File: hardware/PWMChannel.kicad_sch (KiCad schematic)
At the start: 4 parts, among them Q201 IQE006NE2LM5CGSC

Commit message: Refresh
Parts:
- C201: footprint Capacitor_SMD:C_0603_1608Metric -> V2_Capacitor_SMD:C_0603; symbol Device:C_Small -> V2_Device:C_0603_0u1; Manufacturer (none) -> TDK; Mouser (none) -> 810-CGA3E2X7R1H104MA; Product (none) -> CGA3E2X7R1H104M080AA
- D201: footprint Diode_SMD:D_SOD-123F -> V2_Diode_SMD:D_SOD-123F; Manufacturer (none) -> onsemi; Mouser (none) -> 512-S310FA; Product (none) -> S310FA
- D202: LCSC (none) -> C965555; Manufacturer (none) -> Worldsemi; Product (none) -> WS2812B-2020
- Q201: value IQE006NE2LM5CGSC -> IQE022N06LM5CGSCATMA1; symbol V2_Transistor_FET:IQE006NE2LM5CGSC -> V2_Transistor_FET:IQE022N06LM5CGSCATMA1; Manufacturer (none) -> Infineon Technologies; Mouser (none) -> 726-IQE006NE2LM5CGSC; Product (none) -> IQE006NE2LM5CGSCATMA1
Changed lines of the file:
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@@
 			)
 		)
-		(property "Footprint" "Diode_SMD:D_SOD-123F"
+		(property "Footprint" "V2_Diode_SMD:D_SOD-123F"
 			(at 139.065 88.9 0)
 			(effects
@@
 		(property "Description" ""
 			(at 146.05 88.9 0)
+			(effects
+				(font
+					(size 1.27 1.27)
+				)
+				(hide yes)
+			)
+		)
+		(property "Mouser" "512-S310FA"
+			(at 130.81 88.9 0)
+			(effects
+				(font
+					(size 1.27 1.27)
+				)
+				(hide yes)
+			)
+		)
+		(property "Manufacturer" "onsemi"
+			(at 135.89 88.9 0)
+			(effects
+				(font
+					(size 1.27 1.27)
+				)
+				(hide yes)
+			)
+		)
+		(property "Product" "S310FA"
+			(at 133.35 88.9 0)
+			(effects
+				(font
+					(size 1.27 1.27)
+				)
+				(hide yes)
+			)
+		)
+		(property "Sim.Pin" ""
+			(at 146.05 88.9 90)
 			(effects
 				(font
@@
 	)
 	(symbol
-		(lib_id "Device:C_Small")
+		(lib_id "V2_Device:C_0603_0u1")
 		(at 133.35 88.9 0)
 		(unit 1)
@@
 			)
 		)
-		(property "Footprint" "Capacitor_SMD:C_0603_1608Metric"
+		(property "Footprint" "V2_Capacitor_SMD:C_0603"
+			(at 133.35 105.918 0)
+			(effects
+				(font
+					(size 1.27 1.27)
+				)
+				(hide yes)
+			)
+		)
+		(property "Datasheet" ""
 			(at 133.35 88.9 0)
 			(effects
@@
 			)
 		)
-		(property "Datasheet" "~"
-			(at 133.35 88.9 0)
-			(effects
-				(font
-					(size 1.27 1.27)
-				)
-				(hide yes)
-			)
-		)
 		(property "Description" "Unpolarized capacitor, small symbol"
+			(at 133.35 101.6 0)
+			(effects
+				(font
+					(size 1.27 1.27)
+				)
+				(hide yes)
+			)
+		)
+		(property "Mouser" "810-CGA3E2X7R1H104MA"
+			(at 133.35 109.22 0)
+			(show_name yes)
+			(effects
+				(font
+					(size 1.27 1.27)
+				)
+				(hide yes)
+			)
+		)
+		(property "Manufacturer" "TDK"
+			(at 133.35 104.14 0)
+			(show_name yes)
+			(effects
+				(font
+					(size 1.27 1.27)
+				)
+				(hide yes)
+			)
+		)
+		(property "Product" "CGA3E2X7R1H104M080AA"
+			(at 133.35 106.68 0)
+			(show_name yes)
+			(effects
+				(font
+					(size 1.27 1.27)
+				)
+				(hide yes)
+			)
+		)
+		(property "Sim.Pin" ""
 			(at 133.35 88.9 0)
 			(effects
@@
 	)
 	(symbol
-		(lib_id "V2_Transistor_FET:IQE006NE2LM5CGSC")
+		(lib_id "V2_Transistor_FET:IQE022N06LM5CGSCATMA1")
 		(at 130.81 96.52 0)
 		(unit 1)
@@
 			)
 		)
-		(property "Value" "IQE006NE2LM5CGSC"
-			(at 137.16 98.425 0)
+		(property "Value" "IQE022N06LM5CGSCATMA1"
+			(at 137.16 98.044 0)
 			(effects
 				(font
@@
 		)
 		(property "Description" ""
+			(at 130.81 96.52 0)
+			(effects
+				(font
+					(size 1.27 1.27)
+				)
+				(hide yes)
+			)
+		)
+		(property "Mouser" "726-IQE006NE2LM5CGSC"
+			(at 130.81 119.38 0)
+			(effects
+				(font
+					(size 1.27 1.27)
+				)
+				(hide yes)
+			)
+		)
+		(property "Product" "IQE006NE2LM5CGSCATMA1"
+			(at 130.81 116.84 0)
+			(effects
+				(font
+					(size 1.27 1.27)
+				)
+				(hide yes)
+			)
+		)
+		(property "Manufacturer" "Infineon Technologies"
+			(at 130.81 114.3 0)
+			(effects
+				(font
+					(size 1.27 1.27)
+				)
+				(hide yes)
+			)
+		)
+		(property "Sim.Pin" ""
 			(at 130.81 96.52 0)
 			(effects
@@
 	)
 	(symbol
-		(lib_id "power:GND")
+		(lib_id "V2_power:GND")
 		(at 160.02 127 90)
 		(unit 1)
@@
 			)
 		)
+		(property "Manufacturer" "Worldsemi"
+			(at 152.4 141.224 0)
+			(effects
+				(font
+					(size 1.27 1.27)
+				)
+				(hide yes)
+			)
+		)
+		(property "Product" "WS2812B-2020"
+			(at 152.4 138.684 0)
+			(effects
+				(font
+					(size 1.27 1.27)
+				)
+				(hide yes)
+			)
+		)
+		(property "LCSC" "C965555"
+			(at 152.4 144.018 0)
+			(effects
+				(font
+					(size 1.27 1.27)
+				)
+				(hide yes)
+			)
+		)
+		(property "Sim.Pin" ""
+			(at 152.4 125.73 0)
+			(effects
+				(font
+					(size 1.27 1.27)
+				)
+				(hide yes)
+			)
+		)
 		(pin "1"
 		)
@@
 	)
 	(symbol
-		(lib_id "power:GND")
+		(lib_id "V2_power:GND")
 		(at 133.35 101.6 0)
 		(unit 1)
@@
 	)
 	(symbol
-		(lib_id "power:+5V")
+		(lib_id "V2_power:+5V")
 		(at 160.02 121.92 270)
 		(unit 1)

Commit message: Refresh
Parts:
- Q201: value IQE022N06LM5CGSCATMA1 -> IQE006NE2LM5CGSC; symbol V2_Transistor_FET:IQE022N06LM5CGSCATMA1 -> V2_Transistor_FET:IQE006NE2LM5CGSC; Polarity (none) -> N; Product IQE006NE2LM5CGSCATMA1 -> IQE006NE2LM5CGSC; Rating (none) -> 25V
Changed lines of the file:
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@@
-			)
-		)
-		(property "Sim.Pin" ""
-			(at 146.05 88.9 90)
-			(effects
-				(font
-					(size 1.27 1.27)
-				)
-				(hide yes)
 			)
 		)
@@
 			)
 		)
-		(property "Sim.Pin" ""
-			(at 133.35 88.9 0)
-			(effects
-				(font
-					(size 1.27 1.27)
-				)
-				(hide yes)
-			)
-		)
 		(pin "1"
 		)
@@
 	)
 	(symbol
-		(lib_id "V2_Transistor_FET:IQE022N06LM5CGSCATMA1")
+		(lib_id "V2_Transistor_FET:IQE006NE2LM5CGSC")
 		(at 130.81 96.52 0)
 		(unit 1)
@@
 			)
 		)
-		(property "Value" "IQE022N06LM5CGSCATMA1"
-			(at 137.16 98.044 0)
+		(property "Value" "IQE006NE2LM5CGSC"
+			(at 135.89 96.52 0)
 			(effects
 				(font
@@
 		)
 		(property "Footprint" "V2_Package_TFN:WHTFN-9"
-			(at 135.89 98.425 0)
-			(effects
-				(font
-					(size 1.27 1.27)
-				)
-				(justify left)
+			(at 130.81 113.03 0)
+			(show_name yes)
+			(effects
+				(font
+					(size 1.27 1.27)
+				)
 				(hide yes)
 			)
@@
 		)
 		(property "Mouser" "726-IQE006NE2LM5CGSC"
+			(at 130.81 124.46 0)
+			(show_name yes)
+			(effects
+				(font
+					(size 1.27 1.27)
+				)
+				(hide yes)
+			)
+		)
+		(property "Product" "IQE006NE2LM5CGSC"
+			(at 130.81 121.92 0)
+			(show_name yes)
+			(effects
+				(font
+					(size 1.27 1.27)
+				)
+				(hide yes)
+			)
+		)
+		(property "Manufacturer" "Infineon Technologies"
 			(at 130.81 119.38 0)
-			(effects
-				(font
-					(size 1.27 1.27)
-				)
-				(hide yes)
-			)
-		)
-		(property "Product" "IQE006NE2LM5CGSCATMA1"
-			(at 130.81 116.84 0)
-			(effects
-				(font
-					(size 1.27 1.27)
-				)
-				(hide yes)
-			)
-		)
-		(property "Manufacturer" "Infineon Technologies"
-			(at 130.81 114.3 0)
+			(show_name yes)
 			(effects
 				(font
@@
 		(property "Sim.Pin" ""
 			(at 130.81 96.52 0)
+			(effects
+				(font
+					(size 1.27 1.27)
+				)
+				(hide yes)
+			)
+		)
+		(property "Rating" "25V"
+			(at 130.81 116.84 0)
+			(effects
+				(font
+					(size 1.27 1.27)
+				)
+				(hide yes)
+			)
+		)
+		(property "Polarity" "N"
+			(at 130.81 114.3 0)
 			(effects
 				(font
@@
 			(effects
 				(font
-					(size 1.27 1.27)
-				)
-				(hide yes)
-			)
-		)
-		(property "Sim.Pin" ""
-			(at 152.4 125.73 0)
-			(effects
-				(font

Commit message: Update library
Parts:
- C201: Rating (none) -> 50V
- Q201: value IQE006NE2LM5CGSC -> IQE006NE2LM5CG; symbol V2_Transistor_FET:IQE006NE2LM5CGSC -> V2_Transistor_FET:IQE006NE2LM5CG; Mouser 726-IQE006NE2LM5CGSC -> 726-IQE006NE2LM5CGAT; Product IQE006NE2LM5CGSC -> IQE006NE2LM5CG
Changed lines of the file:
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@@
+			)
+		)
+		(property "Sim.Pin" ""
+			(at 146.05 88.9 90)
+			(effects
+				(font
+					(size 1.27 1.27)
+				)
+				(hide yes)
+			)
+		)
+		(property "Voltage" ""
+			(at 146.05 88.9 90)
+			(effects
+				(font
+					(size 1.27 1.27)
+				)
+				(hide yes)
 			)
 		)
@@
 			)
 		)
+		(property "Rating" "50V"
+			(at 133.35 111.76 0)
+			(effects
+				(font
+					(size 1.27 1.27)
+				)
+				(hide yes)
+			)
+		)
+		(property "Sim.Pin" ""
+			(at 133.35 88.9 0)
+			(effects
+				(font
+					(size 1.27 1.27)
+				)
+				(hide yes)
+			)
+		)
+		(property "Voltage" ""
+			(at 133.35 88.9 0)
+			(effects
+				(font
+					(size 1.27 1.27)
+				)
+				(hide yes)
+			)
+		)
 		(pin "1"
 		)
@@
 	)
 	(symbol
-		(lib_id "V2_Transistor_FET:IQE006NE2LM5CGSC")
+		(lib_id "V2_Transistor_FET:IQE006NE2LM5CG")
 		(at 130.81 96.52 0)
 		(unit 1)
@@
 			)
 		)
-		(property "Value" "IQE006NE2LM5CGSC"
-			(at 135.89 96.52 0)
+		(property "Value" "IQE006NE2LM5CG"
+			(at 137.16 98.044 0)
 			(effects
 				(font
@@
 			)
 		)
-		(property "Mouser" "726-IQE006NE2LM5CGSC"
+		(property "Mouser" "726-IQE006NE2LM5CGAT"
 			(at 130.81 124.46 0)
 			(show_name yes)
@@
 			)
 		)
-		(property "Product" "IQE006NE2LM5CGSC"
+		(property "Product" "IQE006NE2LM5CG"
 			(at 130.81 121.92 0)
 			(show_name yes)
@@
 			)
 		)
+		(property "Rating" "25V"
+			(at 130.81 116.84 0)
+			(show_name yes)
+			(effects
+				(font
+					(size 1.27 1.27)
+				)
+				(hide yes)
+			)
+		)
+		(property "Polarity" "N"
+			(at 130.81 114.3 0)
+			(show_name yes)
+			(effects
+				(font
+					(size 1.27 1.27)
+				)
+				(hide yes)
+			)
+		)
 		(property "Sim.Pin" ""
 			(at 130.81 96.52 0)
@@
 			)
 		)
-		(property "Rating" "25V"
-			(at 130.81 116.84 0)
-			(effects
-				(font
-					(size 1.27 1.27)
-				)
-				(hide yes)
-			)
-		)
-		(property "Polarity" "N"
-			(at 130.81 114.3 0)
+		(property "Voltage" ""
+			(at 130.81 96.52 0)
 			(effects
 				(font
@@
 			)
 		)
-		(property "Description" "Power symbol creates a global label with name \"GND\" , ground"
+		(property "Description" ""
 			(at 160.02 127 0)
 			(effects
@@
 			)
 		)
+		(property "Sim.Pin" ""
+			(at 152.4 125.73 0)
+			(effects
+				(font
+					(size 1.27 1.27)
+				)
+				(hide yes)
+			)
+		)
+		(property "Voltage" ""
+			(at 152.4 125.73 0)
+			(effects
+				(font
+					(size 1.27 1.27)
+				)
+				(hide yes)
+			)
+		)
 		(pin "1"
 		)
@@
 			)
 		)
-		(property "Description" "Power symbol creates a global label with name \"GND\" , ground"
+		(property "Description" ""
 			(at 133.35 101.6 0)
 			(effects
@@
 			)
 		)
-		(property "Description" "Power symbol creates a global label with name \"+5V\""
+		(property "Description" ""
 			(at 160.02 121.92 0)
 			(effects

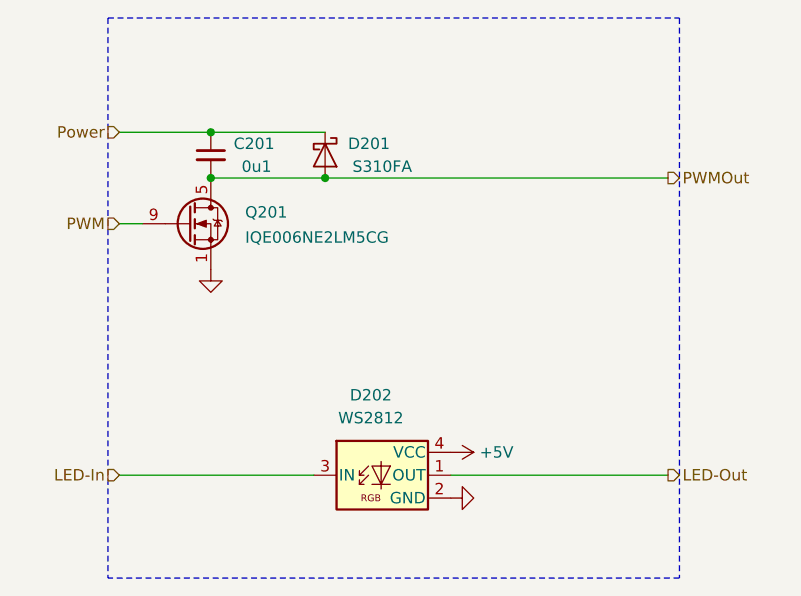
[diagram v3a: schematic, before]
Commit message: Replace Order_Number
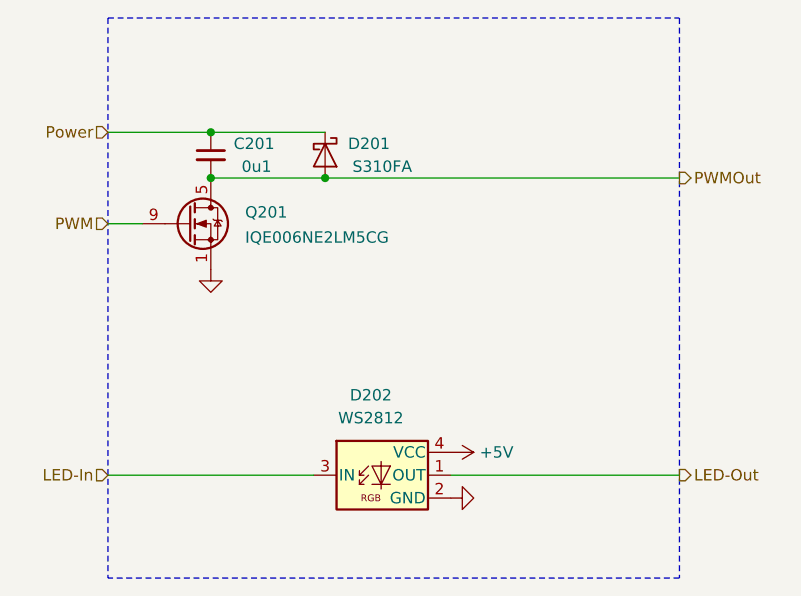
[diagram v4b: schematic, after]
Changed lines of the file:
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@@
 	(title_block
 		(title "Solenoid Channel")
-		(date "2023-01-16")
-		(rev "1")
+		(date "2026-02-10")
+		(rev "2026-02-10")
 		(company "Power MOSFET + RGB LED")
 	)
@@
 	(wire
 		(pts
-			(xy 123.19 96.52) (xy 125.73 96.52)
+			(xy 121.92 96.52) (xy 125.73 96.52)
 		)
 		(stroke
@@
 	(wire
 		(pts
-			(xy 184.15 124.46) (xy 160.02 124.46)
+			(xy 185.42 124.46) (xy 160.02 124.46)
 		)
 		(stroke
@@
 	(wire
 		(pts
-			(xy 123.19 86.36) (xy 133.35 86.36)
+			(xy 121.92 86.36) (xy 133.35 86.36)
 		)
 		(stroke
@@
 	(wire
 		(pts
-			(xy 146.05 91.44) (xy 184.15 91.44)
+			(xy 146.05 91.44) (xy 185.42 91.44)
 		)
 		(stroke
@@
 	(wire
 		(pts
-			(xy 123.19 124.46) (xy 144.78 124.46)
+			(xy 121.92 124.46) (xy 144.78 124.46)
 		)
 		(stroke
@@
 	(hierarchical_label "PWMOut"
 		(shape output)
-		(at 184.15 91.44 0)
+		(at 185.42 91.44 0)
 		(effects
 			(font
@@
 	(hierarchical_label "Power"
 		(shape input)
-		(at 123.19 86.36 180)
+		(at 121.92 86.36 180)
 		(effects
 			(font
@@
 	(hierarchical_label "LED-In"
 		(shape input)
-		(at 123.19 124.46 180)
+		(at 121.92 124.46 180)
 		(effects
 			(font
@@
 	(hierarchical_label "PWM"
 		(shape input)
-		(at 123.19 96.52 180)
+		(at 121.92 96.52 180)
 		(effects
 			(font
@@
 	(hierarchical_label "LED-Out"
 		(shape output)
-		(at 184.15 124.46 0)
+		(at 185.42 124.46 0)
 		(effects
 			(font
@@
 			)
 		)
-		(property "Sim.Pin" ""
-			(at 146.05 88.9 90)
-			(effects
-				(font
-					(size 1.27 1.27)
-				)
-				(hide yes)
-			)
-		)
-		(property "Voltage" ""
-			(at 146.05 88.9 90)
-			(effects
-				(font
-					(size 1.27 1.27)
-				)
-				(hide yes)
-			)
-		)
 		(pin "1"
 		)
@@
 			)
 		)
-		(property "Sim.Pin" ""
-			(at 133.35 88.9 0)
-			(effects
-				(font
-					(size 1.27 1.27)
-				)
-				(hide yes)
-			)
-		)
-		(property "Voltage" ""
-			(at 133.35 88.9 0)
-			(effects
-				(font
-					(size 1.27 1.27)
-				)
-				(hide yes)
-			)
-		)
 		(pin "1"
 		)
@@
 			)
 		)
-		(property "Sim.Pin" ""
-			(at 130.81 96.52 0)
-			(effects
-				(font
-					(size 1.27 1.27)
-				)
-				(hide yes)
-			)
-		)
-		(property "Voltage" ""
-			(at 130.81 96.52 0)
-			(effects
-				(font
-					(size 1.27 1.27)
-				)
-				(hide yes)
-			)
-		)
 		(pin "1"
 		)
@@
 			(effects
 				(font
-					(size 1.27 1.27)
-				)
-				(hide yes)
-			)
-		)
-		(property "Sim.Pin" ""
-			(at 152.4 125.73 0)
-			(effects
-				(font
-					(size 1.27 1.27)
-				)
-				(hide yes)
-			)
-		)
-		(property "Voltage" ""
-			(at 152.4 125.73 0)
-			(effects
-				(font

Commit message: Update Library
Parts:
- C201: symbol V2_Device:C_0603_0u1 -> V2_Capacitor:0603_0u1
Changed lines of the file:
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@@
 	)
 	(symbol
-		(lib_id "V2_Device:C_0603_0u1")
+		(lib_id "V2_Capacitor:0603_0u1")
 		(at 133.35 88.9 0)
 		(unit 1)
@@
 		(on_board yes)
 		(dnp no)
-		(property "Reference" "#PWR0203"
+		(property "Reference" "#PWR203"
 			(at 166.37 127 0)
 			(effects
@@
 			(project "beat"
 				(path "/6c8448b4-b04d-47e1-934e-e40cbe27a7be/20fe3b49-6fc0-49b3-882e-b60ec2c37622"
-					(reference "#PWR0403")
+					(reference "#PWR403")
 					(unit 1)
 				)
 				(path "/6c8448b4-b04d-47e1-934e-e40cbe27a7be/6b0ff6e6-8459-48b3-ad82-b75391ec7027"
-					(reference "#PWR0203")
+					(reference "#PWR203")
 					(unit 1)
 				)
 				(path "/6c8448b4-b04d-47e1-934e-e40cbe27a7be/d14b4538-8a69-4c12-9312-e76942186e04"
-					(reference "#PWR0503")
+					(reference "#PWR503")
 					(unit 1)
 				)
 				(path "/6c8448b4-b04d-47e1-934e-e40cbe27a7be/e8fd4e45-6455-499e-826d-b4439d3dc293"
-					(reference "#PWR0303")
+					(reference "#PWR303")
 					(unit 1)
 				)
@@
 		(on_board yes)
 		(dnp no)
-		(property "Reference" "#PWR0201"
+		(property "Reference" "#PWR201"
 			(at 133.35 107.95 0)
 			(effects
@@
 			(project "beat"
 				(path "/6c8448b4-b04d-47e1-934e-e40cbe27a7be/20fe3b49-6fc0-49b3-882e-b60ec2c37622"
-					(reference "#PWR0401")
+					(reference "#PWR401")
 					(unit 1)
 				)
 				(path "/6c8448b4-b04d-47e1-934e-e40cbe27a7be/6b0ff6e6-8459-48b3-ad82-b75391ec7027"
-					(reference "#PWR0201")
+					(reference "#PWR201")
 					(unit 1)
 				)
 				(path "/6c8448b4-b04d-47e1-934e-e40cbe27a7be/d14b4538-8a69-4c12-9312-e76942186e04"
-					(reference "#PWR0501")
+					(reference "#PWR501")
 					(unit 1)
 				)
 				(path "/6c8448b4-b04d-47e1-934e-e40cbe27a7be/e8fd4e45-6455-499e-826d-b4439d3dc293"
-					(reference "#PWR0301")
+					(reference "#PWR301")
 					(unit 1)
 				)
@@
 		(on_board yes)
 		(dnp no)
-		(property "Reference" "#PWR0202"
+		(property "Reference" "#PWR202"
 			(at 156.21 121.92 0)
 			(effects
@@
 			(project "beat"
 				(path "/6c8448b4-b04d-47e1-934e-e40cbe27a7be/20fe3b49-6fc0-49b3-882e-b60ec2c37622"
-					(reference "#PWR0402")
+					(reference "#PWR402")
 					(unit 1)
 				)
 				(path "/6c8448b4-b04d-47e1-934e-e40cbe27a7be/6b0ff6e6-8459-48b3-ad82-b75391ec7027"
-					(reference "#PWR0202")
+					(reference "#PWR202")
 					(unit 1)
 				)
 				(path "/6c8448b4-b04d-47e1-934e-e40cbe27a7be/d14b4538-8a69-4c12-9312-e76942186e04"
-					(reference "#PWR0502")
+					(reference "#PWR502")
 					(unit 1)
 				)
 				(path "/6c8448b4-b04d-47e1-934e-e40cbe27a7be/e8fd4e45-6455-499e-826d-b4439d3dc293"
-					(reference "#PWR0302")
-					(unit 1)
-				)
+					(reference "#PWR302")
+					(unit 1)
+				)

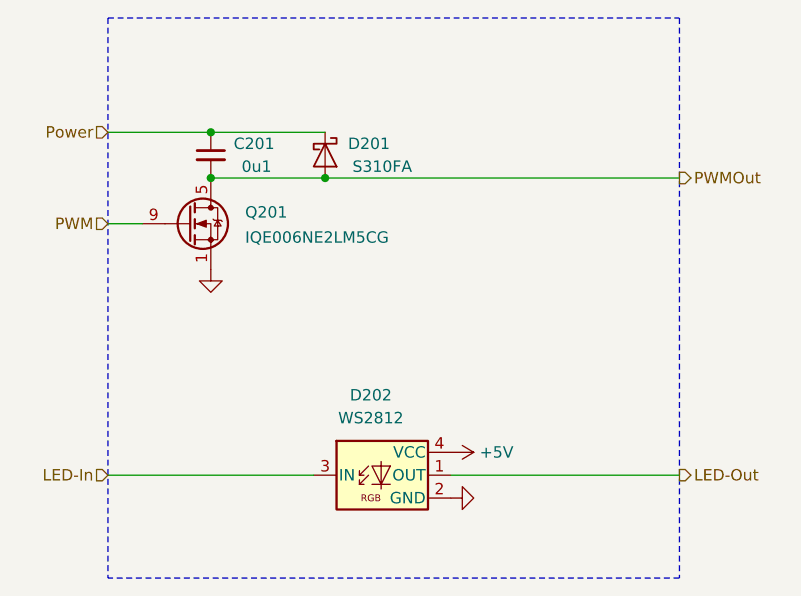
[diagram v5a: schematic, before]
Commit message: Replace diode
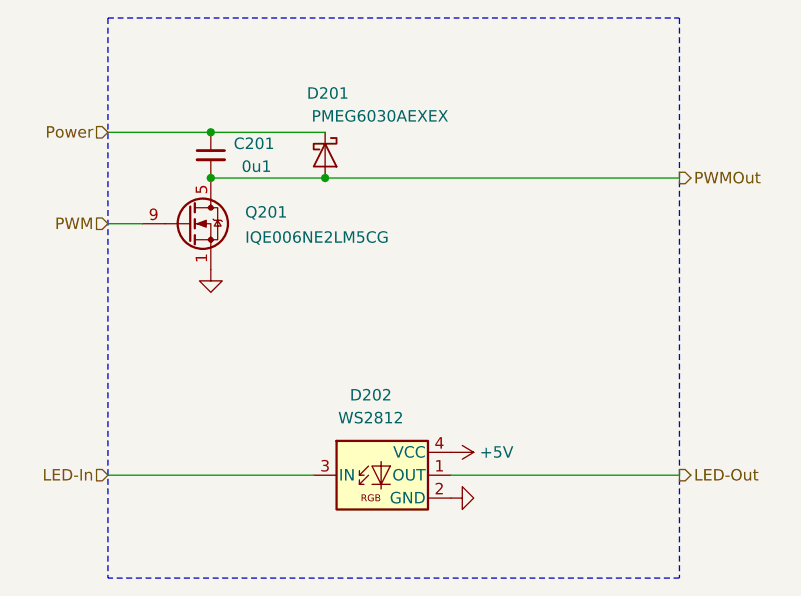
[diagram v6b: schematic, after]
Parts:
- D201: value S310FA -> PMEG6030AEXEX; footprint V2_Diode_SMD:D_SOD-123F -> V2_Diode_SMD:D_SOD-123HP; symbol V2_Diode:S310FA -> V2_Diode:PMEG6030AEXEX; Manufacturer onsemi -> Nexperia; Mouser 512-S310FA -> 771-PMEG6030AEXEX; Product S310FA -> PMEG6030AEXEX
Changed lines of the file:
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@@
 	(title_block
 		(title "Solenoid Channel")
-		(date "2026-02-10")
-		(rev "2026-02-10")
+		(date "2026-03-11")
+		(rev "2026-03-11")
 		(company "Power MOSFET + RGB LED")
 	)
@@
 	)
 	(symbol
-		(lib_id "V2_Diode:S310FA")
+		(lib_id "V2_Diode:PMEG6030AEXEX")
 		(at 146.05 88.9 270)
 		(unit 1)
@@
 		(dnp no)
 		(property "Reference" "D201"
-			(at 148.59 87.63 90)
+			(at 144.018 82.042 90)
 			(effects
 				(font
@@
 			)
 		)
-		(property "Value" "S310FA"
-			(at 152.4 90.17 90)
-			(effects
-				(font
-					(size 1.27 1.27)
-				)
-			)
-		)
-		(property "Footprint" "V2_Diode_SMD:D_SOD-123F"
+		(property "Value" "PMEG6030AEXEX"
+			(at 152.146 84.582 90)
+			(effects
+				(font
+					(size 1.27 1.27)
+				)
+			)
+		)
+		(property "Footprint" "V2_Diode_SMD:D_SOD-123HP"
 			(at 139.065 88.9 0)
 			(effects
@@
 			)
 		)
-		(property "Mouser" "512-S310FA"
+		(property "Mouser" "771-PMEG6030AEXEX"
 			(at 130.81 88.9 0)
 			(effects
@@
 			)
 		)
-		(property "Manufacturer" "onsemi"
+		(property "Manufacturer" "Nexperia"
 			(at 135.89 88.9 0)
 			(effects
@@
 			)
 		)
-		(property "Product" "S310FA"
+		(property "Product" "PMEG6030AEXEX"
 			(at 133.35 88.9 0)
 			(effects
@@
 			)
 		)
-		(property "Description" "Unpolarized capacitor, small symbol"
+		(property "Description" ""
 			(at 133.35 101.6 0)
 			(effects

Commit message: Update ESD suppressor
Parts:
- D201: Rating (none) -> 60V
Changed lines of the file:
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@@
+			)
+		)
+		(property "Rating" "60V"
+			(at 128.27 88.9 0)
+			(effects
+				(font
+					(size 1.27 1.27)
+				)
+				(hide yes)
 			)
 		)

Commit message: Replace diode
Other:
- title: Solenoid Channel -> V2 beat
